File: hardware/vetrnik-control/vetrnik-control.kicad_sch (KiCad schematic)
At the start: 89 parts, among them J1 Conn_01x20_Male, J10 Conn_01x04, J11 Conn_01x03_Male, J12 Conn_02x04_Odd_Even, J13 Conn_02x04_Odd_Even, J14 Conn_02x04_Odd_Even, J15 Conn_01x04, J16 Conn_01x04, J17 Conn_01x04, J18 Conn_01x03, J19 Conn_01x04, J2 Conn_01x04, J20 Conn_01x04, J3 Conn_01x03, J4 Conn_02x04_Odd_Even, J5 Conn_02x04_Odd_Even, J6 Conn_02x04_Odd_Even, J7 Conn_01x20_Male, J8 Screw_Terminal_01x02, J9 Conn_01x03, Q1 BC857, Q2 BC847, Q3 BC847, Q4 BC847, Q5 BSS138, Q6 BSS138, Q7 BC847, Q8 BSS138, SW1 SW_Push, SW2 SW_Push, U1 LTV-817S, U2 YAAJ_WeAct_BlackPill_Part_Like, U3 MX25L8006EM1I-12G, U4 WIZ850io

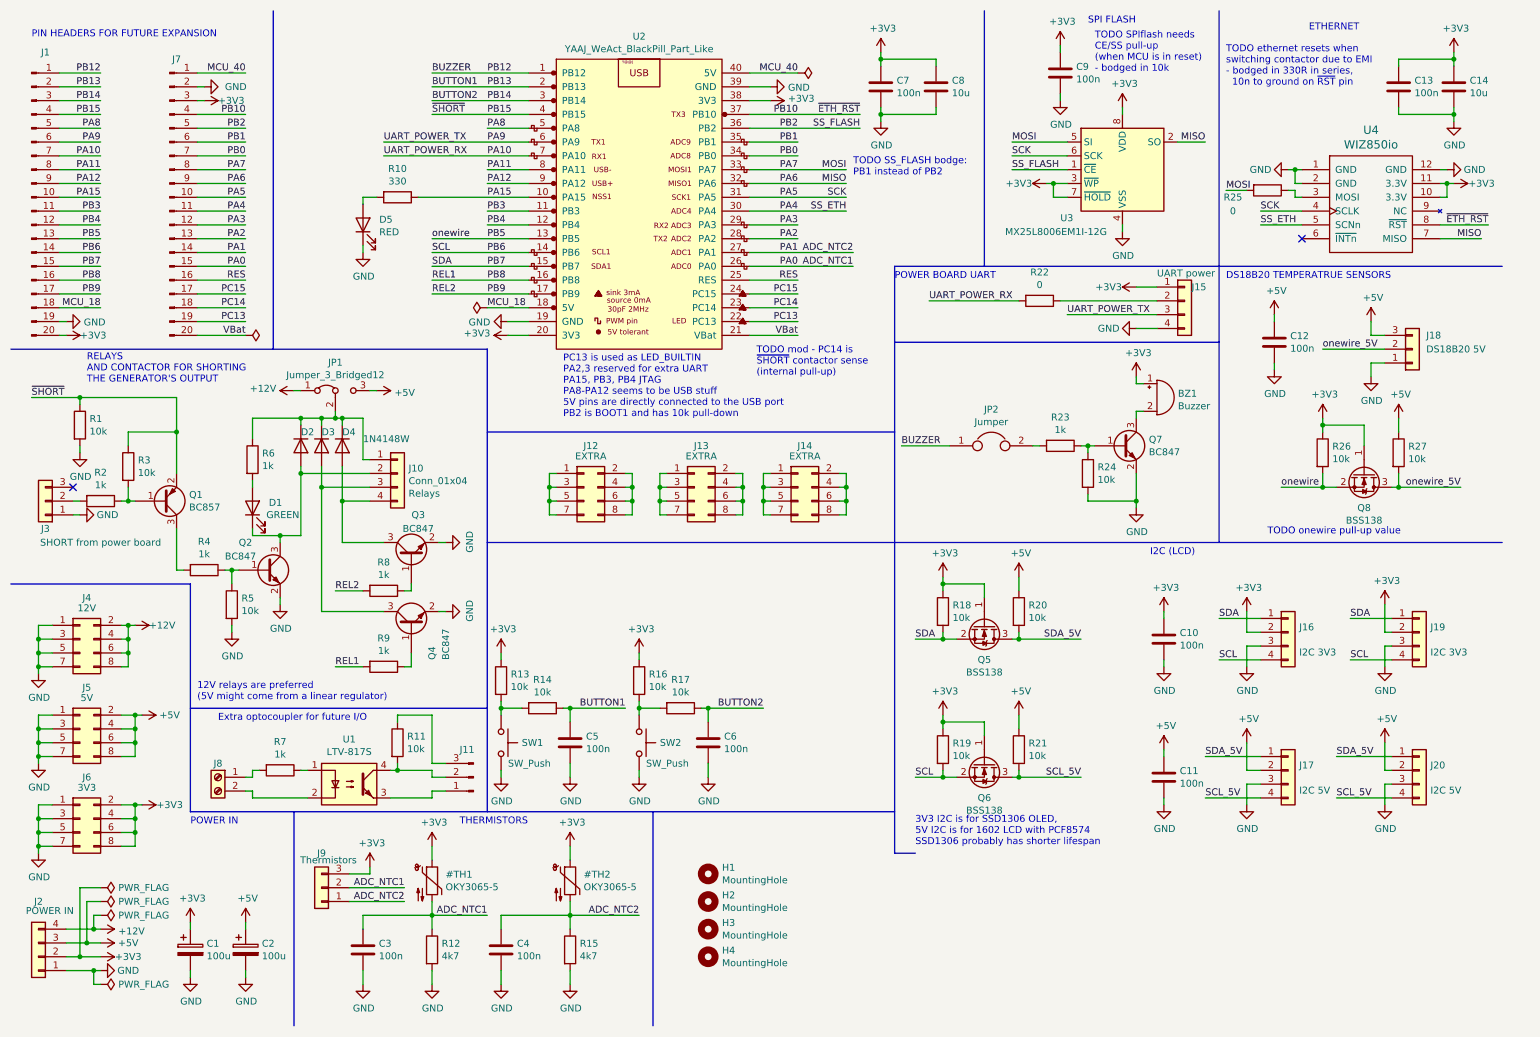
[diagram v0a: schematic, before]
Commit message: [hardwa] Add info about hardware mods
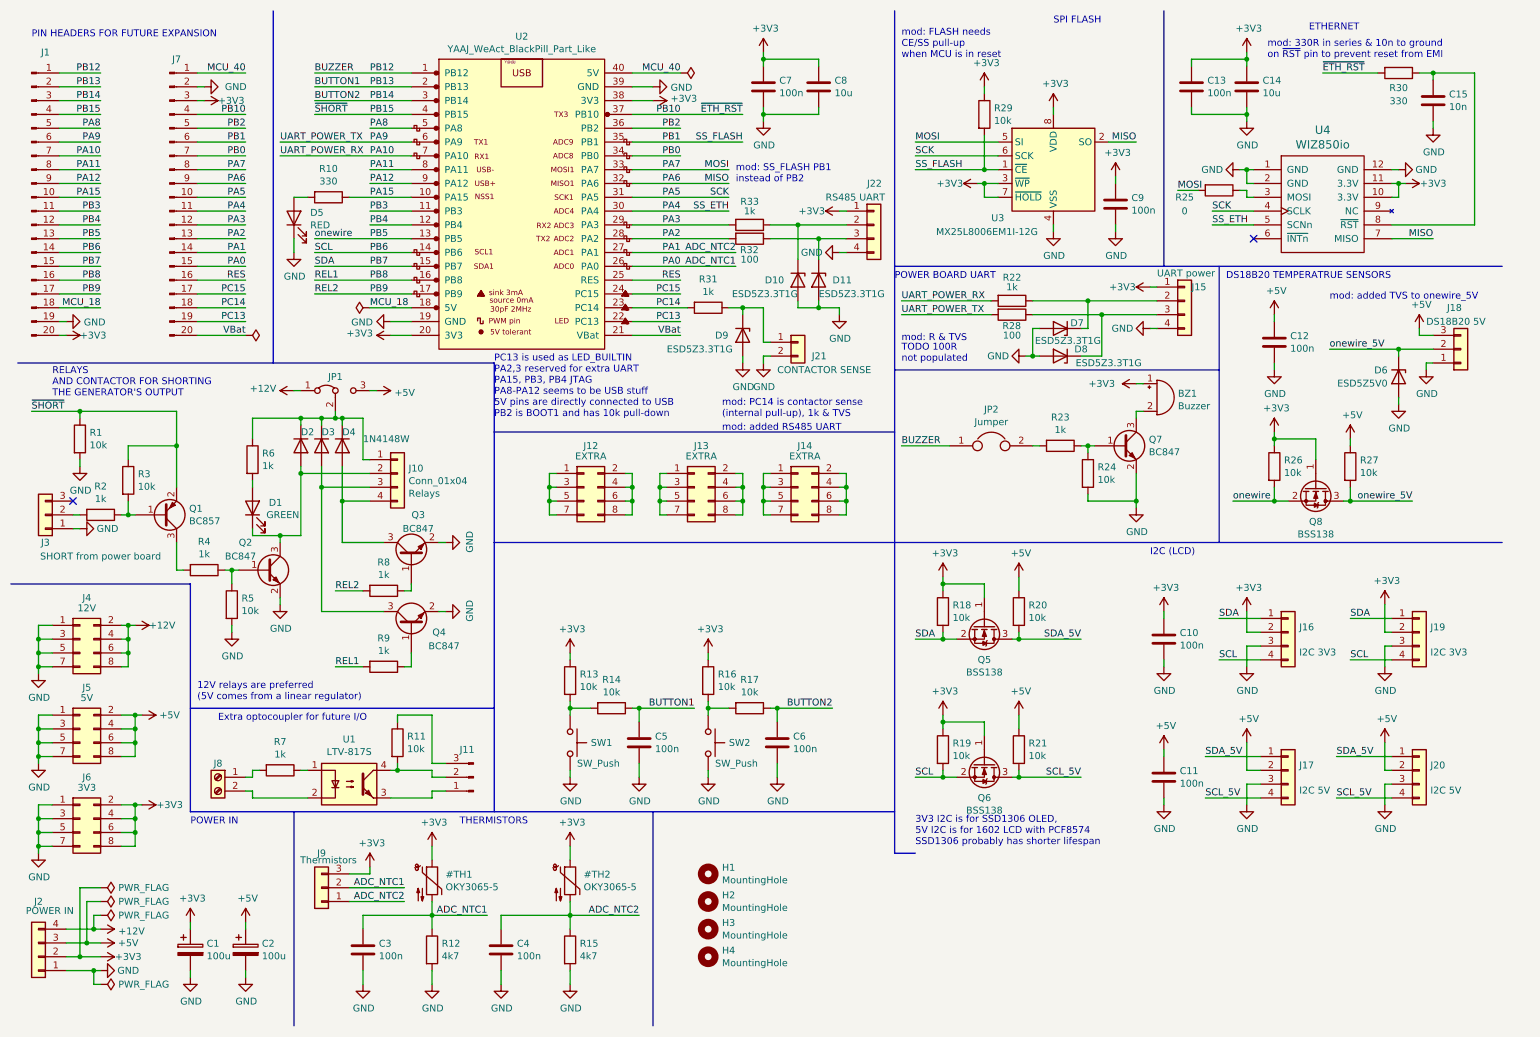
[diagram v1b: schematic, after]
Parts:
- added C15: 10n, Capacitor_SMD:C_1206_3216Metric_Pad1.33x1.80mm_HandSolder, symbol Device:C
- added D10, D11, D7, D8, D9: ESD5Z3.3T1G, Diode_SMD:D_SOD-523, symbol Diode:ESD5Zxx
- added D6: ESD5Z5V0, Diode_SMD:D_SOD-523, symbol Diode:ESD5Zxx
- added J21: Conn_01x02, symbol Connector_Generic:Conn_01x02
- added J22: Conn_01x04, symbol Connector_Generic:Conn_01x04
- added R28, R32: 100, Resistor_SMD:R_1206_3216Metric_Pad1.30x1.75mm_HandSolder, symbol Device:R
- added R29: 10k, Resistor_SMD:R_1206_3216Metric_Pad1.30x1.75mm_HandSolder, symbol Device:R
- added R30: 330, Resistor_SMD:R_1206_3216Metric_Pad1.30x1.75mm_HandSolder, symbol Device:R
- added R31, R33: 1k, Resistor_SMD:R_1206_3216Metric_Pad1.30x1.75mm_HandSolder, symbol Device:R
- R22: value 0 -> 1k
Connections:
- net +3V3: now also J22.1 (Pin_1), R29.1
- net GND: now also C15.2, D10.2 (A), D11.2 (A), D6.2 (A), D7.2 (A), D8.2 (A), D9.2 (A), J21.2 (Pin_2), J22.4 (Pin_4)
- net PA2: now also R32.2
- net PA3: now also R33.2
- net PA9: now also R28.2; no longer J15.3 (Pin_3)
- net PB1: now also U3.1 (~{CE}), R29.2
- net PB10: now also R30.2; no longer U4.8 (~{RST})
- net PB2: no longer U3.1 (~{CE})
- net PC14: now also R31.2
- net onewire_5V: now also D6.1 (K)
- net at J15.2 (Pin_2), R22.1: now also D7.1 (K)
- new net: D8.1 (K), J15.3 (Pin_3), R28.1
- new net: C15.1, R30.1, U4.8 (~{RST})
- new net: D9.1 (K), J21.1 (Pin_1), R31.1
- new net: D10.1 (K), J22.2 (Pin_2), R33.1
- new net: D11.1 (K), J22.3 (Pin_3), R32.1
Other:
- note added: "12V relays are preferred (5V comes from a linear regulator)"
- note added: "PC13 is used as LED_BUILTIN PA2,3 reserved for extra UART PA15, PB3, PB4 JTAG PA8-PA12 seems to be USB stuff 5V pins are directly connected to USB PB2 is BOOT1 and has 10k pull-down"
- note added: "TODO 100R not populated"
- note added: "mod: 330R in series & 10n to ground on ~{RST} pin to prevent reset from EMI"
- note added: "mod: FLASH needs CE/SS pull-up when MCU is in reset"
- note added: "mod: PC14 is contactor sense (internal pull-up), 1k & TVS"
- note added: "mod: R & TVS"
- note added: "mod: SS_FLASH PB1 instead of PB2"
- note added: "mod: added RS485 UART"
- note added: "mod: added TVS to onewire_5V"
- note removed: "12V relays are preferred (5V might come from a linear regulator)"
- note removed: "PC13 is used as LED_BUILTIN PA2,3 reserved for extra UART PA15, PB3, PB4 JTAG PA8-PA12 seems to be USB stuff 5V pins are directly connected to the USB port PB2 is BOOT1 and has 10k pull-down"
- note removed: "TODO SPIflash needs CE/SS pull-up (when MCU is in reset) - bodged in 10k"
- note removed: "TODO SS_FLASH bodge: PB1 instead of PB2"
- note removed: "TODO ethernet resets when switching contactor due to EMI - bodged in 330R in series, 10n to ground on ~{RST} pin"
- note removed: "TODO mod - PC14 is ~{SHORT} contactor sense (internal pull-up)"
- note removed: "TODO onewire pull-up value"
- moved on the sheet: C13, C14, C5, C6, C7, C8, C9, D5, J18, J3, Q1, Q8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

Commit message: [hardware] Clean up vetrnik-control
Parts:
- removed J22: Conn_01x04, symbol Connector_Generic:Conn_01x04
- added J22: Conn_01x05, symbol Connector_Generic:Conn_01x05
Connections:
- net +3V3: now also J22.1 (Pin_1)
- net GND: now also J22.5 (Pin_5)
- net PB0: now also J22.4 (Pin_4)
- net RS485_RX: now reaches D10.1 (K), R33.1
- net RS485_RX: now also J22.2 (Pin_2)
- net RS485_TX: now reaches D11.1 (K), R32.1
- net RS485_TX: now also J22.3 (Pin_3)
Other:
- note added: "(Altough the signal is still named SHORT, the contactor no longer shorts the generator, but rather disconnects it.)"
- note added: "PC13 is used as LED_BUILTIN PA15, PB3, PB4 JTAG PA8-PA12 USB 5V pins are directly connected to USB PB2 is BOOT1 and has 10k pull-down"
- note added: "RC filter on ~{ETH_RST} needed to prevent reset from EMI."
- note added: "RELAYS AND CONTACTOR"
- note removed: "PC13 is used as LED_BUILTIN PA2,3 reserved for extra UART PA15, PB3, PB4 JTAG PA8-PA12 seems to be USB stuff 5V pins are directly connected to USB PB2 is BOOT1 and has 10k pull-down"
- note removed: "RELAYS AND CONTACTOR FOR SHORTING THE GENERATOR'S OUTPUT"
- note removed: "TODO 100R not populated"
- note removed: "mod: 330R in series & 10n to ground on ~{RST} pin to prevent reset from EMI"
- note removed: "mod: FLASH needs CE/SS pull-up when MCU is in reset"
- note removed: "mod: PC14 is contactor sense (internal pull-up), 1k & TVS"
- note removed: "mod: R & TVS"
- note removed: "mod: SS_FLASH PB1 instead of PB2"
- note removed: "mod: added RS485 UART"
- note removed: "mod: added TVS to onewire_5V"
- title: (none) -> vetrnik-control
- moved on the sheet: J12, J13, J14
